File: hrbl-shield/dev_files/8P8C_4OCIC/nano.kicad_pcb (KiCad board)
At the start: 2 copper layers, 80 x 169.5 mm, 47 parts, among them J1 8P8C_Shielded SIG, J2 8P8C_Shielded X, J3 8P8C_Shielded Y, J4 8P8C_Shielded Y2, J5 8P8C_Shielded Z, P1 Digital, P2 Analog, U1 LTV-844, U15 IFX27001TFV50ATMA1CT-ND, U2 LTV-844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

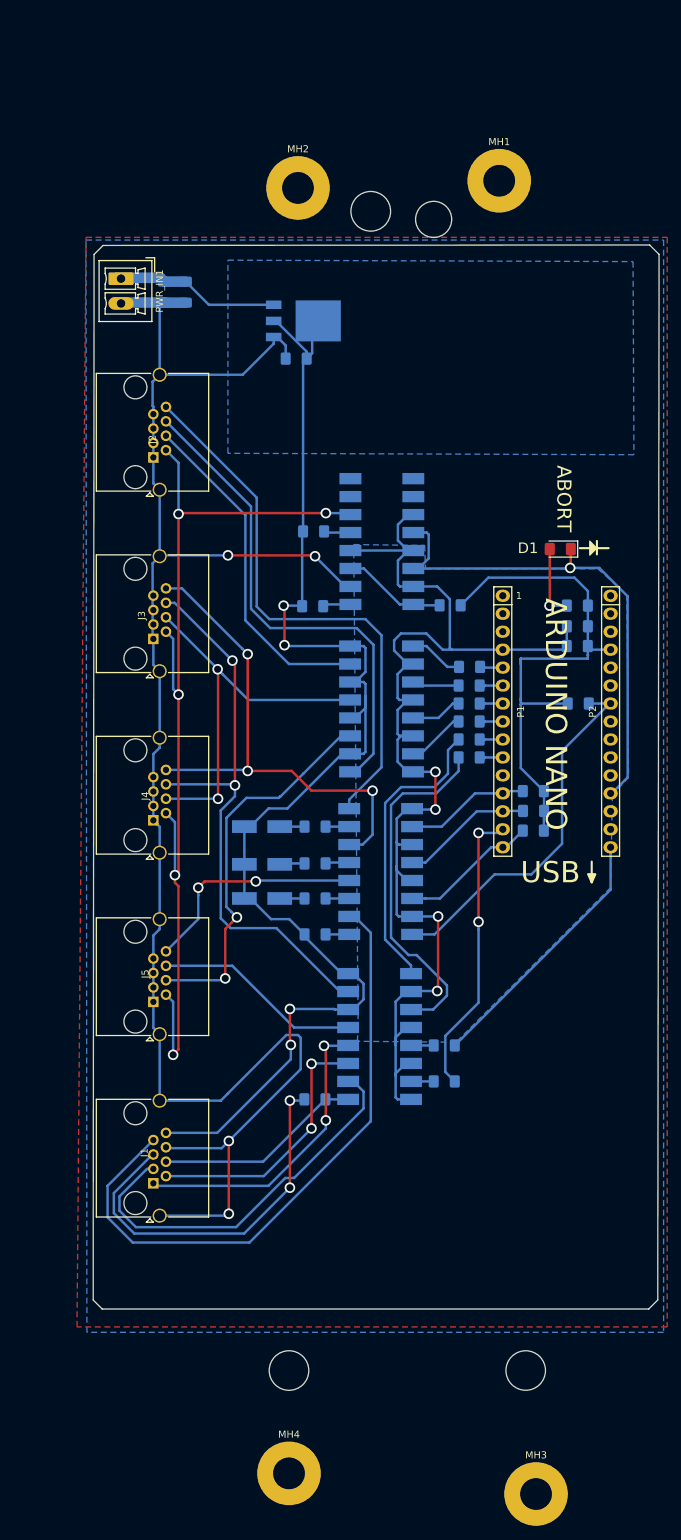
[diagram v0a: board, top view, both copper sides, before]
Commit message: Moved arduino to corner and added spindle alarm
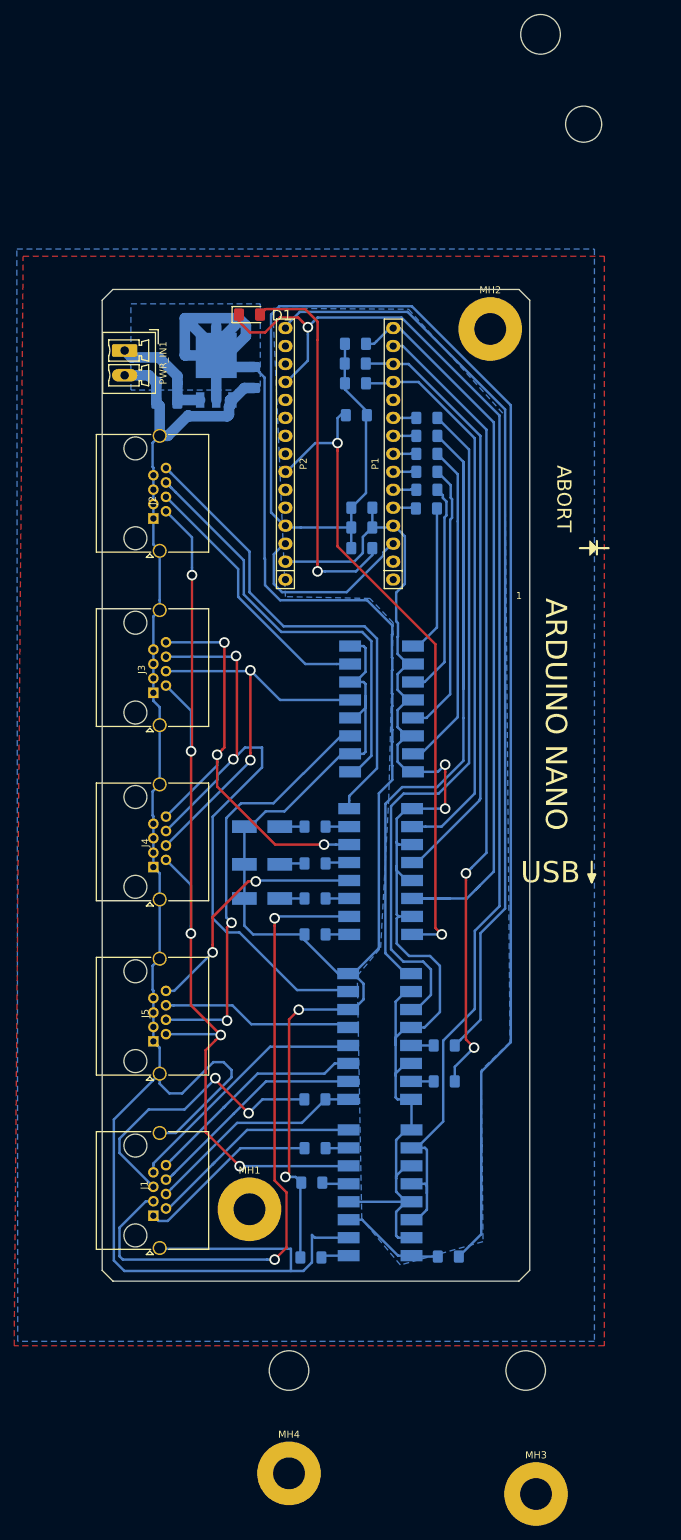
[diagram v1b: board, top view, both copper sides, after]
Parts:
- added R16: 220, Resistor_SMD:R_1206_3216Metric_Pad1.42x1.75mm_HandSolder, B.Cu at (112.9, 149.4)
- moved MH1 149.6 mm to (103.6, 158.0)
- moved R12 92.1 mm to (112.3, 164.8)
- moved R15 92.1 mm to (131.7, 164.7)
- moved U1 92.1 mm to (122.1, 155.7)
- moved R13 92.1 mm to (112.4, 154.2)
- moved R25 73.3 mm to (118.6, 35.6), turned to 0 degrees
- moved R24 68.1 mm to (118.6, 38.4), turned to 0 degrees
- moved R23 62.9 mm to (118.6, 41.2), turned to 0 degrees
- moved D1 55.0 mm to (103.6, 31.5), turned to 0 degrees
- moved R26 51.4 mm to (118.7, 45.7), turned to 180 degrees
- moved R9 48.4 mm to (128.7, 46.1), turned to 180 degrees
- moved P2 46.0 mm to (108.7, 69.0), turned to 90 degrees
- moved R8 43.3 mm to (128.7, 48.6), turned to 180 degrees
- moved R7 38.3 mm to (128.7, 51.2), turned to 180 degrees
- moved C6 36.2 mm to (119.5, 58.8), turned to 180 degrees
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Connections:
- net Net-(R15-Pad1) renamed /Invert
- J1 pad 1: SOURCE_FOR -> ALARM_EXTRA_1
- J1 pad 2: GND_FOR -> ALARM_EXTRA_2
- J1 pad 3: SOURCE_SPEED -> PROBE_PLATE
- J1 pad 6: GNDS -> SOURCE_SPEED
- J1 pad 7: PROBE_PLATE -> SOURCE_FOR
- J1 pad 8: 5V_ISO -> GND_FOR
- U1 pad 10: (no net) -> ABORT
- U1 pad 7: (no net) -> Net-(R16-Pad1)
- U1 pad 8: (no net) -> ALARM_EXTRA_2
- U1 pad 9: (no net) -> GND
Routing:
- net +5V: track 76.6 -> 236.9 mm
- net ABORT: track 73.7 -> 182.9 mm
- net SPINDLE_EN: track 37.1 -> 131.4 mm
- net 5V_ISO: track 196.4 -> 288.7 mm, vias 4 -> 2
- net LIM_Z: track 19.6 -> 107.6 mm
- net Net-(R8-Pad1): track 41.7 -> 119.0 mm
- net SPINDLE_PWM: track 41.3 -> 113.0 mm
- net LIM_Y: track 18.9 -> 85.4 mm
- net LIM_X: track 17.7 -> 80.2 mm
- net Net-(R9-Pad1): track 50.2 -> 98.6 mm
- net Net-(D1-Pad2): track 10.5 -> 54.2 mm
- net PROBE: track 52.8 -> 94.4 mm, vias 0 -> 2
- net Net-(R7-Pad1): track 8.35 -> 46.9 mm
- net Net-(R6-Pad1): track 7.30 -> 39.1 mm
- net ALARM_EXTRA_2: track 0.00 -> 30.8 mm
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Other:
- board size 80 x 169.5 mm -> 70.6 x 194.5 mm
